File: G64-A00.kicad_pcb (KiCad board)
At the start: 2 copper layers, 390 x 179.8 mm, 231 parts, among them CN1 KEYBOARD_20PIN_MALE, CN10 LED_CONNECTOR, CN2 USER_PORT_CON, CN3 CASSETTE_PORT_CON, CN4 SERIAL_BUS_CON, CN5 AV_CONN, CN6 EXPANSION_PORT, CN7 POWER_CON, CN8 CONTROL_PORT, CN9 CONTROL_PORT, M1 MODULATOR_LONGBOARD, Q1 2SC1815, Q2 2SC1815, Q3 TP29B/2SD880, Q7 2SC1815, Q8 2SC1815, SW1 POWER_SWITCH, U1 CIA_U1, U10 4164-2, U11 4164-2, U12 4164-2, U13 74LS257, U14 74LS258, U15 74LS139, U16 4066_U28, U17 PLA_U17, U18 6581, U19 VIC, U2 CIA_U2, U20 556, U21 4164-2, U22 4164-2, U23 4164-2, U24 4164-2, U25 74LS257, U26 74LS373, U27 7408_U27, U28 4066_U28, U29 74LS74, U3 2364A, U30 74LS193, U31 74LS629N, U32 MC4044, U4 2364A, U5 2332A, U6 2114, U7 6510_MPU, U8 7406N, U9 4164-2, Y1 Crystal

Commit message: update edge connectors
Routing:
- net /9V_IN': track 50.5 -> 65.7 mm
- net GND: track 2339.5 -> 2354.0 mm
- net CAN+5V: track 287.3 -> 292.4 mm
- net +12V: track 285.1 -> 281.0 mm
- net /9VAC': track 423.8 -> 426.5 mm
- net /CASS_WRT': track 53.2 -> 50.8 mm
- net /9VAC: track 532.6 -> 534.9 mm
- net D2: track 664.4 -> 663.0 mm
- net +5V: track 2307.5 -> 2306.2 mm
- net /CASS_RD: track 260.8 -> 259.7 mm
- net /CASS_PWR: track 50.7 -> 49.9 mm
- net /CASS_SENSE: track 185.3 -> 184.6 mm

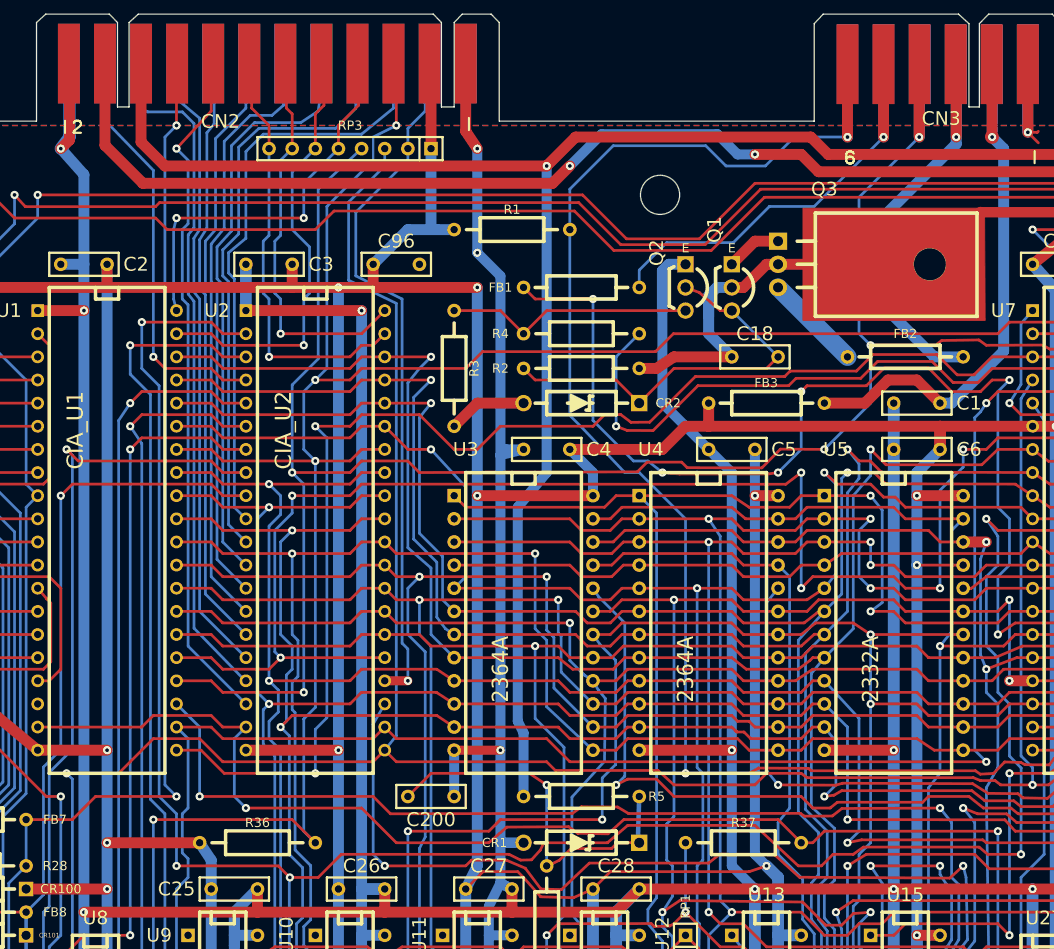
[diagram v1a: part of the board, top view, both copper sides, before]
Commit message: remove EMI ferrite beads
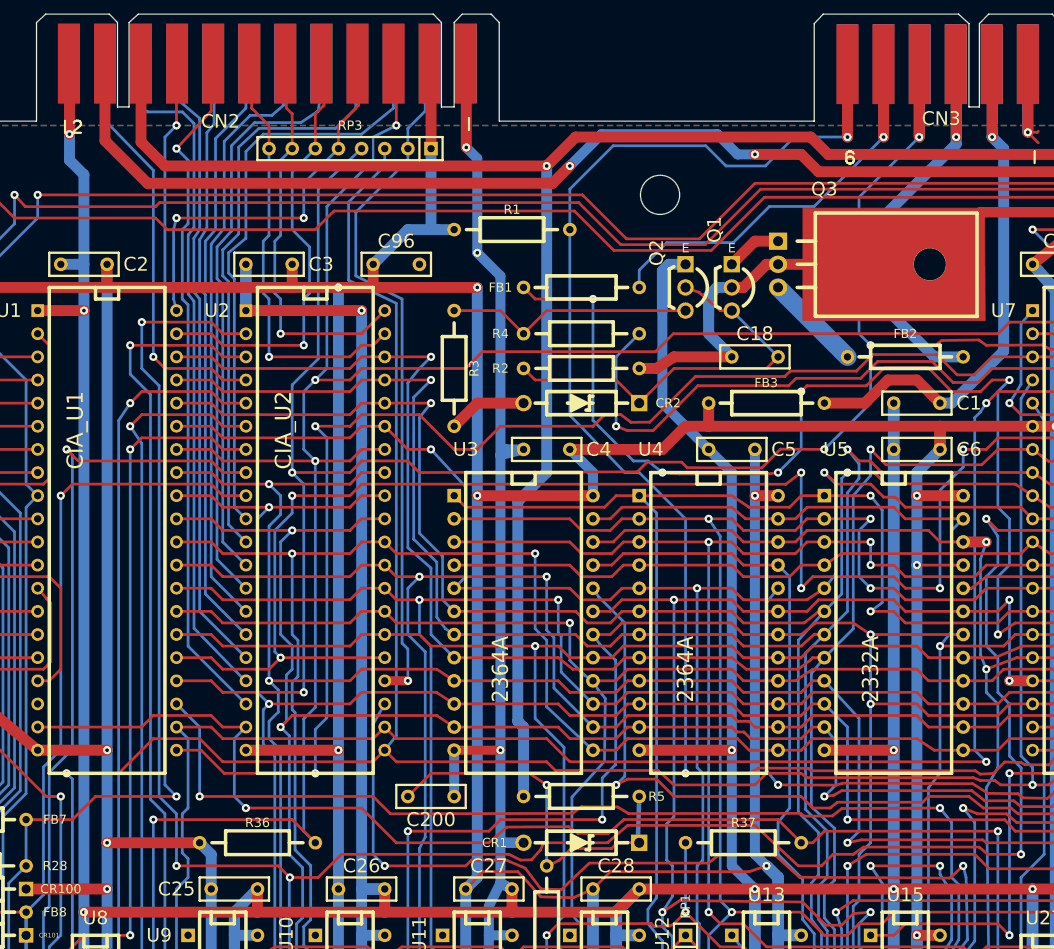
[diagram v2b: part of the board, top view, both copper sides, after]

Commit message: replace discrete clock generation with MOS8701
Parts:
- removed C107, C108: 10uF, pth_cp:CP_5p2x11
- removed C36: 20pF, C64-pcb-library:RESISTOR
- removed C56, C67, C68, C74, C82, C84: .1, pth_c:C_film_7x2.5
- removed C70: 15pF 5%, C64-pcb-library:RESISTOR
- removed C83, C86: 82pF, C64-pcb-library:RESISTOR
- removed C85: .47, pth_c:C_film_7x2.5
- removed E2: JUMPER_WIRE_DASHED, C64-pcb-library:JUMPER_WIRE
- removed FB1, FB13, FB14, FB15, FB16, FB17, FB18, FB19, FB2, FB20, FB21, FB23, FB3, FB4, FB5, FB7, FB8, FB9: FERRITE_BEAD, C64-pcb-library:FERRITE_BEAD_TH_P12.7mm
- removed L2: 2.2uH, C64-pcb-library:RESISTOR
- removed Q7: 2SC1815, C64-pcb-library:Q_NPN_ECB
- removed R16: 1K, pth_r:r_0250p12_7
- removed R17: 2K7, pth_r:r_0250p12_7
- removed R19: 15K, pth_r:r_0250p12_7
- removed R26, R53: 100, pth_r:r_0250p12_7
- removed R27: 500, C64-pcb-library:POTMETER
- removed R52: 330, pth_r:r_0250p12_7
- removed U29: 74LS74, pth_dil:DIP-14_300
- removed U30: 74LS193, pth_dil:DIP-16_300
- removed U32: MC4044, pth_dil:DIP-14_300
- added C58: .22uF, pth_c:C_film_7x2.5, F.Cu at (273.1, 155.6)
- added CT1: 22pF, C64-pcb-library:CAP_trim_5.08mm, F.Cu at (293.4, 169.5)
- added L1: L, C64-pcb-library:RESISTOR, F.Cu at (289.6, 175.9)
- added R60: 100, pth_r:r_0250p12_7, F.Cu at (96.5, 81.3)
- C66: value .1 -> .1uF
- E1: footprint C64-pcb-library:JUMPER_WIRE -> pin_strip:pin_strip_2
- U31: value 74LS629N -> 8701
- Y1: footprint C64-pcb-library:CRYSTAL -> xtal:XTAL_PTH_HC-49US
- moved C65 39.5 mm to (303.5, 189.9), turned to 180 degrees
- moved C66 35.2 mm to (299.7, 181.0)
- moved C60 33.5 mm to (284.5, 145.4), turned to 270 degrees
- moved C50 33.0 mm to (194.3, 150.5), turned to 270 degrees
- moved E1 30.4 mm to (264.8, 177.2), turned to 270 degrees
- moved FB22 28.0 mm to (295.9, 142.9)
- moved C94 25.3 mm to (237.5, 191.1), turned to 90 degrees
- moved FB10 23.0 mm to (200.7, 165.7)
- moved FB12 20.8 mm to (237.5, 179.7), turned to 270 degrees
- moved C53 18.5 mm to (232.4, 183.5), turned to 90 degrees
- moved Y1 13.5 mm to (286.4, 167.0), turned to 270 degrees
- moved C101 13.2 mm to (262.3, 145.4), turned to 270 degrees
- moved C52 11.7 mm to (201.9, 142.9)
- moved C62 10.5 mm to (200.7, 153.0)
- moved R39 8.98 mm to (392.4, 202.6), turned to 90 degrees
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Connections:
- C1 pad 1: /5V_FB3 -> +5V
- CN10 pad 2: /GND_LED -> GND
- CN2 pad 9: /ATN' -> /ATN
- CN3 pad B,2: /5V_FB3 -> +5V
- CN6 pad C: /G64-A00_sheet2/~RESET'~ -> ~RESET~
- CN8 pad 7: /5V_joyport -> +5V
- CN9 pad 7: /5V_joyport -> +5V
- CR100 pad 2: /DATA' -> /DATA
- CR101 pad 1: /DATA' -> /DATA
- CR102 pad 2: /CLK' -> /CLK
- CR103 pad 1: /CLK' -> /CLK
- E1 pad 1: GND -> Net-(E1-Pad1)
- E1 pad 2: /jumper_select -> GND
- Q3 pad 3: Net-(FB2-Pad2) -> /CASS_PWR
- R28 pad 1: /ATN' -> /ATN
- R29 pad 1: /DATA' -> /DATA
- R30 pad 1: /CLK' -> /CLK
- R39 pad 2: Net-(FB21-Pad1) -> /LED+
- R6 pad 2: Net-(FB13-Pad1) -> Net-(R6-Pad2)
- R7 pad 2: Net-(FB13-Pad2) -> Net-(R6-Pad2)
- U18 pad 27: Net-(FB13-Pad1) -> Net-(R6-Pad2)
- U19 pad 14: Net-(FB14-Pad1) -> /G64-A00_sheet2/CHROMA
- U19 pad 15: Net-(FB15-Pad1) -> /G64-A00_sheet2/LUMA
- U19 pad 17: Net-(FB23-Pad1) -> PHI0
- U2 pad 8: /CLK' -> /CLK
- U2 pad 9: /DATA' -> /DATA
- U31 pad 1: Net-(C108-Pad1) -> (no net)
- U31 pad 10: Net-(FB16-Pad1) -> (no net)
- U31 pad 11: GND -> (no net)
- U31 pad 12: Net-(U31-Pad12) -> Net-(C58-Pad1)
- U31 pad 13: Net-(C70-Pad2) -> Net-(CT1-Pad1)
- U31 pad 14: GND -> Net-(U31-Pad14)
- U31 pad 15: Net-(C107-Pad1) -> Net-(C58-Pad1)
- U31 pad 16: /+Vc -> (no net)
- U31 pad 2: Net-(R16-Pad2) -> GND
- U31 pad 3: GND -> (no net)
- U31 pad 4: Net-(C86-Pad2) -> GND
- U31 pad 5: Net-(C86-Pad1) -> (no net)
- U31 pad 6: GND -> DOT_CLOCK
- U31 pad 7: Net-(FB17-Pad1) -> Net-(E1-Pad1)
- U31 pad 8: GND -> PHI_COLOR
- U7 pad 39: /PH2_FB -> PHI2
- U8 pad 10: /CLK' -> /CLK
- U8 pad 12: /ATN' -> /ATN
- U8 pad 2: /DATA' -> /DATA
- Y1 pad 1: Net-(U31-Pad12) -> Net-(U31-Pad14)
- Y1 pad 2: Net-(C70-Pad1) -> Net-(CT1-Pad1)
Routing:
- net /+Vc: track 275.2 -> 0.00 mm, vias 4 -> 0
- net GND: track 2354.3 -> 2084.0 mm, vias 79 -> 76
- net ~RESET~: track 429.6 -> 625.2 mm, vias 10 -> 12
- net /G64-A00_sheet2/~RESET'~: track 192.6 -> 0.00 mm, vias 1 -> 0
- net CAN+5V: track 292.4 -> 161.9 mm, vias 1 -> 0
- net /CLK: track 262.1 -> 390.1 mm, vias 2 -> 3
- net /ATN': track 127.6 -> 0.00 mm, vias 3 -> 0
- net /CLK': track 117.8 -> 0.00 mm, vias 1 -> 0
- net Net-(R16-Pad2): track 101.8 -> 0.00 mm, vias 1 -> 0
- net /DATA': track 92.1 -> 0.00 mm, vias 1 -> 0
- net /DATA: track 261.0 -> 351.2 mm, vias 2 -> 4
- net +5V: track 2306.6 -> 2391.9 mm, vias 30 -> 31
- net PHI0: track 282.9 -> 199.0 mm, vias 8 -> 4
- net /5V_joyport: track 82.3 -> 0.00 mm
- net PHI_COLOR: track 98.7 -> 25.4 mm
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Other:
- board text added: "PAL"
